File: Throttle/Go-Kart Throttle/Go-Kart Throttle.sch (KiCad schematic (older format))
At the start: 5 parts, among them J1 Program/Data, U1 ATTiny85

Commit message: Added annotations to schematic
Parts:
- gave numbers to parts that had none: 1
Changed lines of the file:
@@
 	4850 3400 5200 3400
 $Comp
-L Connector:Conn_01x02_Male J?
+L Connector:Conn_01x02_Male J2
 U 1 1 60C8EDB9
 P 750 750
-F 0 "J?" H 858 931 50  0000 C CNN
+F 0 "J2" H 858 931 50  0000 C CNN
 F 1 "Power Input" H 858 840 50  0000 C CNN
 F 2 "" H 750 750 50  0001 C CNN
@@
 $EndComp
 $Comp
-L power:+5V #PWR?
+L power:+5V #PWR07
 U 1 1 60C8FC52
 P 1250 700
-F 0 "#PWR?" H 1250 550 50  0001 C CNN
+F 0 "#PWR07" H 1250 550 50  0001 C CNN
 F 1 "+5V" H 1265 873 50  0000 C CNN
 F 2 "" H 1250 700 50  0001 C CNN
@@
 $EndComp
 $Comp
-L power:GND #PWR?
+L power:GND #PWR08
 U 1 1 60C9028B
 P 1250 900
-F 0 "#PWR?" H 1250 650 50  0001 C CNN
+F 0 "#PWR08" H 1250 650 50  0001 C CNN
 F 1 "GND" H 1255 727 50  0000 C CNN
 F 2 "" H 1250 900 50  0001 C CNN

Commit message: Changed stuff
Added a throttle tester.
Added the wiring schematic for the whole kart and updated schematics for throttle
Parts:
- removed J1: Program/Data, symbol Connector:Conn_01x04_Male
- added C1: 1uF, symbol Device:C
- added J1: Conn_01x05, symbol Connector_Generic:Conn_01x05
- added JP1: Program/Run, symbol Device:Jumper_NO_Small
- added JP?: Jumper_3_Open, symbol Jumper:Jumper_3_Open
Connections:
- net +5V: now also C1.1, JP1.1; no longer U1.1 (RESET)
- net GND: now also C1.2, J1.5 (Pin_5), JP?.3 (B)
- net MISO: now also J1.2 (Pin_2), JP?.2 (C)
- net SCL_SCK: now also J1.1 (Pin_1)
- net SDA_MOSI: now also J1.3 (Pin_3)
- new net: JP1.2, U1.1 (RESET)
- new net RESET: J1.4 (Pin_4)
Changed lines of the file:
@@
 $EndComp
-Wire Wire Line
-	4250 2700 4250 2750
 Wire Wire Line
 	4250 3850 4250 3950
-Wire Wire Line
-	4250 2750 3650 2750
-Wire Wire Line
-	3650 2750 3650 3200
-Wire Wire Line
-	3650 3200 3700 3200
-Connection ~ 4250 2750
-Wire Wire Line
-	4250 2750 4250 2800
 $Comp
 L Device:R_POT RV1
@@
 The wipers face each other and \nthus the connections must be reversed
 $Comp
-L Connector:Conn_01x04_Male J1
-U 1 1 60C84ECC
-P 3100 750
-F 0 "J1" H 3072 724 50  0000 R CNN
-F 1 "Program/Data" H 3072 633 50  0000 R CNN
-F 2 "" H 3100 750 50  0001 C CNN
-F 3 "~" H 3100 750 50  0001 C CNN
-	1    3100 750
-	-1   0    0    -1
-$EndComp
-$Comp
 L power:GND #PWR06
 U 1 1 60C86AC6
-P 2800 1050
-F 0 "#PWR06" H 2800 800 50  0001 C CNN
-F 1 "GND" H 2805 877 50  0000 C CNN
-F 2 "" H 2800 1050 50  0001 C CNN
-F 3 "" H 2800 1050 50  0001 C CNN
-	1    2800 1050
+P 2800 1150
+F 0 "#PWR06" H 2800 900 50  0001 C CNN
+F 1 "GND" H 2805 977 50  0000 C CNN
+F 2 "" H 2800 1150 50  0001 C CNN
+F 3 "" H 2800 1150 50  0001 C CNN
+	1    2800 1150
 	-1   0    0    -1
 $EndComp
 Wire Wire Line
-	2800 1050 2800 950
-Wire Wire Line
-	2800 950  2900 950
+	2800 1150 2800 1050
+Wire Wire Line
+	2800 1050 2900 1050
 Text GLabel 2550 650  0    50   Input ~ 0
 SCL_SCK
@@
 Text GLabel 5200 3300 2    50   Input ~ 0
 MISO
-Text GLabel 5200 3400 2    50   Input ~ 0
+Text GLabel 5200 3550 2    50   Input ~ 0
 SDA_MOSI
 Wire Wire Line
 	4850 3200 5200 3200
 Wire Wire Line
-	5200 3300 4850 3300
-Wire Wire Line
-	4850 3400 5200 3400
+	5200 3300 5100 3300
 $Comp
 L Connector:Conn_01x02_Male J2
@@
 Wire Wire Line
 	1250 850  1250 900
+Wire Wire Line
+	4250 2700 4250 2750
+$Comp
+L Device:Jumper_NO_Small JP1
+U 1 1 60CA881F
+P 3550 2950
+F 0 "JP1" V 3504 2998 50  0000 L CNN
+F 1 "Program/Run" V 3500 2400 50  0000 L CNN
+F 2 "" H 3550 2950 50  0001 C CNN
+F 3 "~" H 3550 2950 50  0001 C CNN
+	1    3550 2950
+	0    1    1    0
+$EndComp
+Wire Wire Line
+	3550 2850 3550 2750
+Wire Wire Line
+	3550 2750 4250 2750
+Connection ~ 4250 2750
+Wire Wire Line
+	4250 2750 4250 2800
+Wire Wire Line
+	3550 3050 3550 3200
+Wire Wire Line
+	3550 3200 3700 3200
+Text GLabel 2550 950  0    50   Input ~ 0
+RESET
+Wire Wire Line
+	2550 950  2900 950
+$Comp
+L Connector_Generic:Conn_01x05 J1
+U 1 1 60CAA1FC
+P 3100 850
+F 0 "J1" H 3180 892 50  0000 L CNN
+F 1 "Conn_01x05" H 3180 801 50  0000 L CNN
+F 2 "" H 3100 850 50  0001 C CNN
+F 3 "~" H 3100 850 50  0001 C CNN
+	1    3100 850
+	1    0    0    -1
+$EndComp
+$Comp
+L Device:C C1
+U 1 1 60CAB591
+P 1550 800
+F 0 "C1" H 1665 846 50  0000 L CNN
+F 1 "1uF" H 1665 755 50  0000 L CNN
+F 2 "" H 1588 650 50  0001 C CNN
+F 3 "~" H 1550 800 50  0001 C CNN
+	1    1550 800
+	1    0    0    -1
+$EndComp
+Wire Wire Line
+	1550 650  1350 650
+Wire Wire Line
+	1350 650  1350 750
+Wire Wire Line
+	1350 750  1250 750
+Connection ~ 1250 750
+Wire Wire Line
+	1550 950  1350 950
+Wire Wire Line
+	1350 950  1350 850
+Wire Wire Line
+	1350 850  1250 850
+Connection ~ 1250 850
+$Comp
+L Jumper:Jumper_3_Open JP?
+U 1 1 60CAD104
+P 4450 1250
+F 0 "JP?" V 4404 1337 50  0000 L CNN
+F 1 "Jumper_3_Open" V 4495 1337 50  0000 L CNN
+F 2 "" H 4450 1250 50  0001 C CNN
+F 3 "~" H 4450 1250 50  0001 C CNN
+	1    4450 1250
+	0    1    1    0
+$EndComp
+Text GLabel 4200 1250 0    50   Input ~ 0
+Orientation
+Wire Wire Line
+	4200 1250 4300 1250
+$Comp
+L power:GND #PWR?
+U 1 1 60CAF6E6
+P 4450 1600
+F 0 "#PWR?" H 4450 1350 50  0001 C CNN
+F 1 "GND" H 4455 1427 50  0000 C CNN
+F 2 "" H 4450 1600 50  0001 C CNN
+F 3 "" H 4450 1600 50  0001 C CNN
+	1    4450 1600
+	-1   0    0    -1
+$EndComp
+Wire Wire Line
+	4450 1500 4450 1600
+Text GLabel 5200 3400 2    50   Input ~ 0
+Orientation
+Wire Wire Line
+	5200 3400 5100 3400
+Wire Wire Line
+	5100 3400 5100 3300
+Connection ~ 5100 3300
+Wire Wire Line
+	5100 3300 4850 3300
+Wire Wire Line
+	5200 3550 4950 3550
+Wire Wire Line
+	4950 3550 4950 3400
+Wire Wire Line
+	4950 3400 4850 3400
 $EndSCHEMATC

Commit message: ggfh
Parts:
- RV1: value Throttle_1 -> Throttle_1/Left
- RV2: value Throttle_2 -> Throttle_2/Right
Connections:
- net +5V: now also RV1.1, RV2.3; no longer RV1.3, RV2.1
- net GND: now also RV1.3, RV2.1; no longer RV1.1, RV2.3
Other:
- note added: "22 - WHT"
- note added: "22 - YLW"
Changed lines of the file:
@@
 P 2050 3150
 F 0 "RV1" H 1981 3196 50  0000 R CNN
-F 1 "Throttle_1" H 1981 3105 50  0000 R CNN
+F 1 "Throttle_1/Left" H 1981 3105 50  0000 R CNN
 F 2 "" H 2050 3150 50  0001 C CNN
 F 3 "~" H 2050 3150 50  0001 C CNN
 	1    2050 3150
-	1    0    0    -1
+	1    0    0    1
 $EndComp
 $Comp
@@
 P 2050 3950
 F 0 "RV2" H 1981 3996 50  0000 R CNN
-F 1 "Throttle_2" H 1981 3905 50  0000 R CNN
+F 1 "Throttle_2/Right" H 1981 3905 50  0000 R CNN
 F 2 "" H 2050 3950 50  0001 C CNN
 F 3 "~" H 2050 3950 50  0001 C CNN
 	1    2050 3950
-	1    0    0    -1
+	1    0    0    1
 $EndComp
 $Comp
@@
 Wire Wire Line
 	4950 3400 4850 3400
+Text Notes 2250 3150 0    50   ~ 0
+22 - WHT
+Text Notes 2250 3950 0    50   ~ 0
+22 - YLW
 $EndSCHEMATC

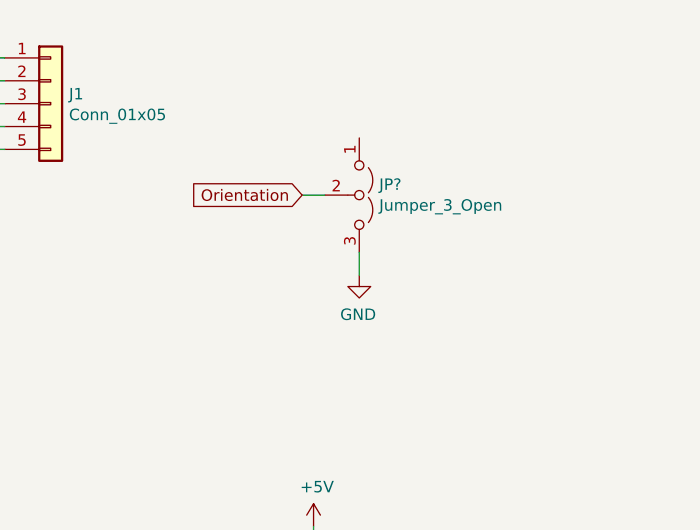
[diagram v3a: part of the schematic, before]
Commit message: Updated schematic and code
Added pulldown resistor instead of direct grounding on MOSI line due to not being able to program it.

Also added EEPROM code to store the calibration to not have to calibrate each time at startup. Calibration can be forced if the throttle is in the full on position when in the normal orientation
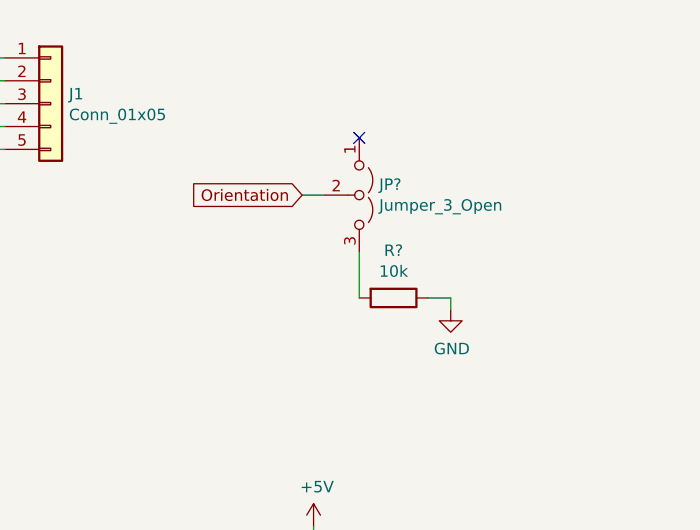
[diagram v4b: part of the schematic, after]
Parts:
- added R?: 10k, symbol Device:R
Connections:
- net GND: now also R?.1; no longer JP?.3 (B)
- new net: JP?.3 (B), R?.2
- no-connect marks 0 -> 1
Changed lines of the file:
@@
 Wire Wire Line
 	4200 1250 4300 1250
-$Comp
-L power:GND #PWR?
-U 1 1 60CAF6E6
-P 4450 1600
-F 0 "#PWR?" H 4450 1350 50  0001 C CNN
-F 1 "GND" H 4455 1427 50  0000 C CNN
-F 2 "" H 4450 1600 50  0001 C CNN
-F 3 "" H 4450 1600 50  0001 C CNN
-	1    4450 1600
-	-1   0    0    -1
-$EndComp
-Wire Wire Line
-	4450 1500 4450 1600
 Text GLabel 5200 3400 2    50   Input ~ 0
 Orientation
@@
 Text Notes 2250 3950 0    50   ~ 0
 22 - YLW
+$Comp
+L Device:R R?
+U 1 1 611701B3
+P 4600 1700
+F 0 "R?" V 4393 1700 50  0000 C CNN
+F 1 "10k" V 4484 1700 50  0000 C CNN
+F 2 "" V 4530 1700 50  0001 C CNN
+F 3 "~" H 4600 1700 50  0001 C CNN
+	1    4600 1700
+	0    1    1    0
+$EndComp
+$Comp
+L power:GND #PWR?
+U 1 1 611706DF
+P 4850 1750
+F 0 "#PWR?" H 4850 1500 50  0001 C CNN
+F 1 "GND" H 4855 1577 50  0000 C CNN
+F 2 "" H 4850 1750 50  0001 C CNN
+F 3 "" H 4850 1750 50  0001 C CNN
+	1    4850 1750
+	1    0    0    -1
+$EndComp
+Wire Wire Line
+	4750 1700 4850 1700
+Wire Wire Line
+	4850 1700 4850 1750
+Wire Wire Line
+	4450 1500 4450 1700
+NoConn ~ 4450 1000
 $EndSCHEMATC
